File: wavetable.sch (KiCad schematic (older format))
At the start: 10 parts, among them J3 LineOut, J6 Wavetable, J7 AuxOut, U10 78L05, U11 79L05, U12 OPA2134

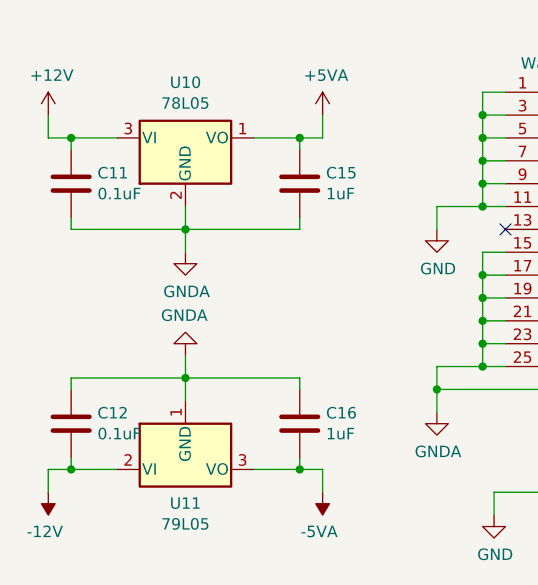
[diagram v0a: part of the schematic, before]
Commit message: Tweak component values
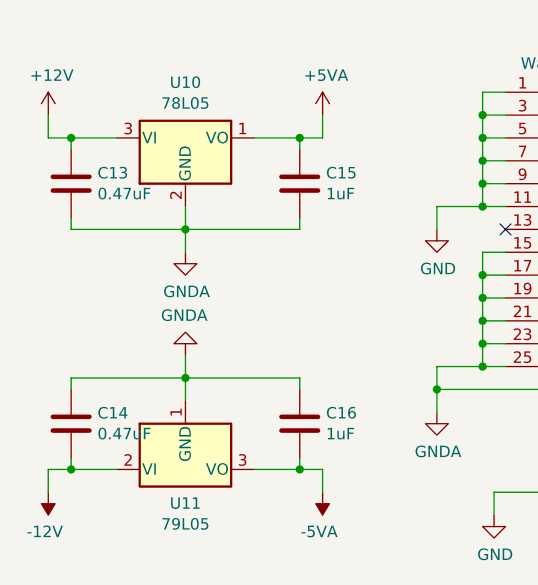
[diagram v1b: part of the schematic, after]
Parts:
- C13: renamed from C11; value 0.1uF -> 0.47uF; footprint Capacitor_THT:C_Disc_D3.0mm_W1.6mm_P2.50mm -> Capacitor_THT:C_Disc_D3.0mm_W2.0mm_P2.50mm
- C14: renamed from C12; value 0.1uF -> 0.47uF; footprint Capacitor_THT:C_Disc_D3.0mm_W1.6mm_P2.50mm -> Capacitor_THT:C_Disc_D3.0mm_W2.0mm_P2.50mm
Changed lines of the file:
@@
 EELAYER 30 0
 EELAYER END
-$Descr A4 11693 8268
+$Descr USLetter 11000 8500
 encoding utf-8
 Sheet 2 2
@@
 	2350 2450 2450 2450
 $Comp
-L Device:C C11
+L Device:C C13
 U 1 1 62784BE7
 P 2450 2650
-F 0 "C11" H 2565 2696 50  0000 L CNN
-F 1 "0.1uF" H 2565 2605 50  0000 L CNN
-F 2 "Capacitor_THT:C_Disc_D3.0mm_W1.6mm_P2.50mm" H 2488 2500 50  0001 C CNN
+F 0 "C13" H 2565 2696 50  0000 L CNN
+F 1 "0.47uF" H 2565 2605 50  0000 L CNN
+F 2 "Capacitor_THT:C_Disc_D3.0mm_W2.0mm_P2.50mm" H 2488 2500 50  0001 C CNN
 F 3 "~" H 2450 2650 50  0001 C CNN
 	1    2450 2650
@@
 	2950 3400 2950 3500
 $Comp
-L Device:C C12
+L Device:C C14
 U 1 1 627A99F4
 P 2450 3700
-F 0 "C12" H 2565 3746 50  0000 L CNN
-F 1 "0.1uF" H 2565 3655 50  0000 L CNN
-F 2 "Capacitor_THT:C_Disc_D3.0mm_W1.6mm_P2.50mm" H 2488 3550 50  0001 C CNN
+F 0 "C14" H 2565 3746 50  0000 L CNN
+F 1 "0.47uF" H 2565 3655 50  0000 L CNN
+F 2 "Capacitor_THT:C_Disc_D3.0mm_W2.0mm_P2.50mm" H 2488 3550 50  0001 C CNN
 F 3 "~" H 2450 3700 50  0001 C CNN
 	1    2450 3700
@@
 	7350 2750 7450 2750
 $Comp
-L power:GNDA #PWR?
+L power:GNDA #PWR0164
 U 1 1 62720331
 P 2950 2950
-F 0 "#PWR?" H 2950 2700 50  0001 C CNN
+F 0 "#PWR0164" H 2950 2700 50  0001 C CNN
 F 1 "GNDA" H 2955 2777 50  0000 C CNN
 F 2 "" H 2950 2950 50  0001 C CNN
@@
 $EndComp
 $Comp
-L power:GNDA #PWR?
+L power:GNDA #PWR0166
 U 1 1 62720CC9
 P 2950 3400
-F 0 "#PWR?" H 2950 3150 50  0001 C CNN
+F 0 "#PWR0166" H 2950 3150 50  0001 C CNN
 F 1 "GNDA" H 2955 3227 50  0000 C CNN
 F 2 "" H 2950 3400 50  0001 C CNN

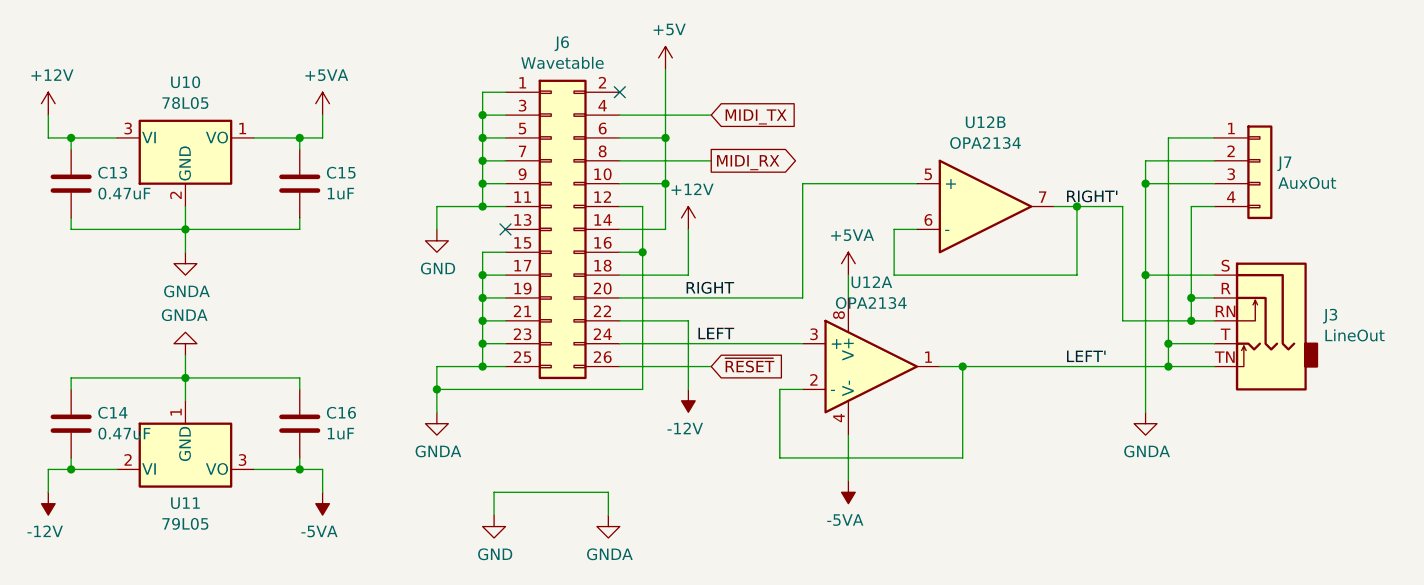
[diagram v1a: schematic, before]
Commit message: Move DA-15 so board aligns with Keystone 9200-11 bracket
Adapt board to fit common Keystone 9200-11, add jumpers to switch wavetable between Internal and External UART
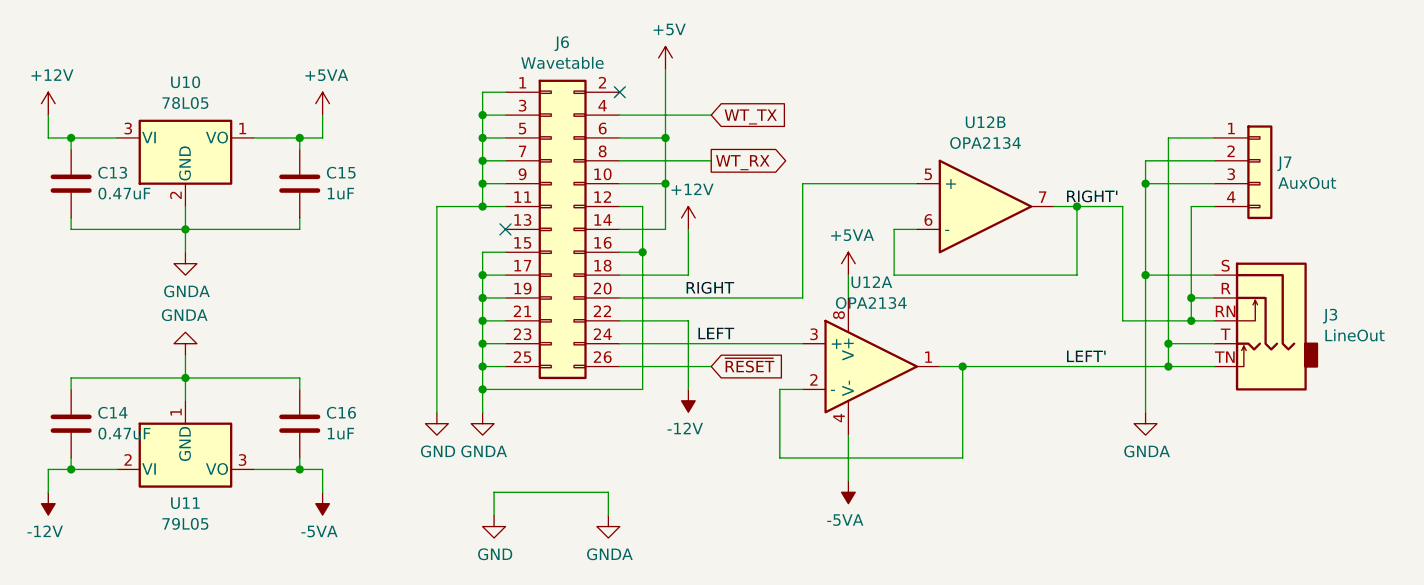
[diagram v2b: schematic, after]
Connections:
- net MIDI_RX renamed WT_RX
- net MIDI_TX renamed WT_TX
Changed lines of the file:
@@
 L power:GND #PWR?
 U 1 1 62624326
-P 4050 2850
+P 4050 3650
 AR Path="/62624326" Ref="#PWR?"  Part="1"
 AR Path="/6262004C/62624326" Ref="#PWR0142"  Part="1"
-F 0 "#PWR0142" H 4050 2600 50  0001 C CNN
-F 1 "GND" H 4055 2677 50  0000 C CNN
-F 2 "" H 4050 2850 50  0001 C CNN
-F 3 "" H 4050 2850 50  0001 C CNN
-	1    4050 2850
-	1    0    0    -1
-$EndComp
-Wire Wire Line
-	4050 2850 4050 2750
-Wire Wire Line
-	4050 2750 4250 2750
-Connection ~ 4250 2750
-$Comp
-L power:GNDA #PWR?
-U 1 1 6262432F
-P 4050 3650
-AR Path="/6262432F" Ref="#PWR?"  Part="1"
-AR Path="/6262004C/6262432F" Ref="#PWR0143"  Part="1"
-F 0 "#PWR0143" H 4050 3400 50  0001 C CNN
-F 1 "GNDA" H 4055 3477 50  0000 C CNN
+F 0 "#PWR0142" H 4050 3400 50  0001 C CNN
+F 1 "GND" H 4055 3477 50  0000 C CNN
 F 2 "" H 4050 3650 50  0001 C CNN
 F 3 "" H 4050 3650 50  0001 C CNN
@@
 $EndComp
 Wire Wire Line
-	4250 3450 4050 3450
-Wire Wire Line
-	4050 3450 4050 3550
-Connection ~ 4250 3450
+	4050 3650 4050 2750
+Wire Wire Line
+	4050 2750 4250 2750
+Connection ~ 4250 2750
+$Comp
+L power:GNDA #PWR?
+U 1 1 6262432F
+P 4250 3650
+AR Path="/6262432F" Ref="#PWR?"  Part="1"
+AR Path="/6262004C/6262432F" Ref="#PWR0143"  Part="1"
+F 0 "#PWR0143" H 4250 3400 50  0001 C CNN
+F 1 "GNDA" H 4255 3477 50  0000 C CNN
+F 2 "" H 4250 3650 50  0001 C CNN
+F 3 "" H 4250 3650 50  0001 C CNN
+	1    4250 3650
+	1    0    0    -1
+$EndComp
 NoConn ~ 4350 2850
 Text Label 5350 3350 2    50   ~ 0
@@
 	7150 3050 7150 3650
 Text GLabel 5250 2350 2    50   Input ~ 0
-MIDI_TX
+WT_TX
 Text GLabel 5250 2550 2    50   Output ~ 0
-MIDI_RX
+WT_RX
 $Comp
 L Device:Opamp_Dual_Generic U12
@@
 	4950 2950 4950 3550
 Wire Wire Line
-	4950 3550 4050 3550
+	4950 3550 4250 3550
 Connection ~ 4950 2950
-Connection ~ 4050 3550
-Wire Wire Line
-	4050 3550 4050 3650
+Wire Wire Line
+	4250 3550 4250 3650
 Wire Wire Line
 	7250 3450 6350 3450
@@
 	-1   0    0    1
 $EndComp
+Wire Wire Line
+	4250 3550 4250 3450
+Connection ~ 4250 3550
+Connection ~ 4250 3450
 $EndSCHEMATC
